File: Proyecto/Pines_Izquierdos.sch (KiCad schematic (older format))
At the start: 7 parts

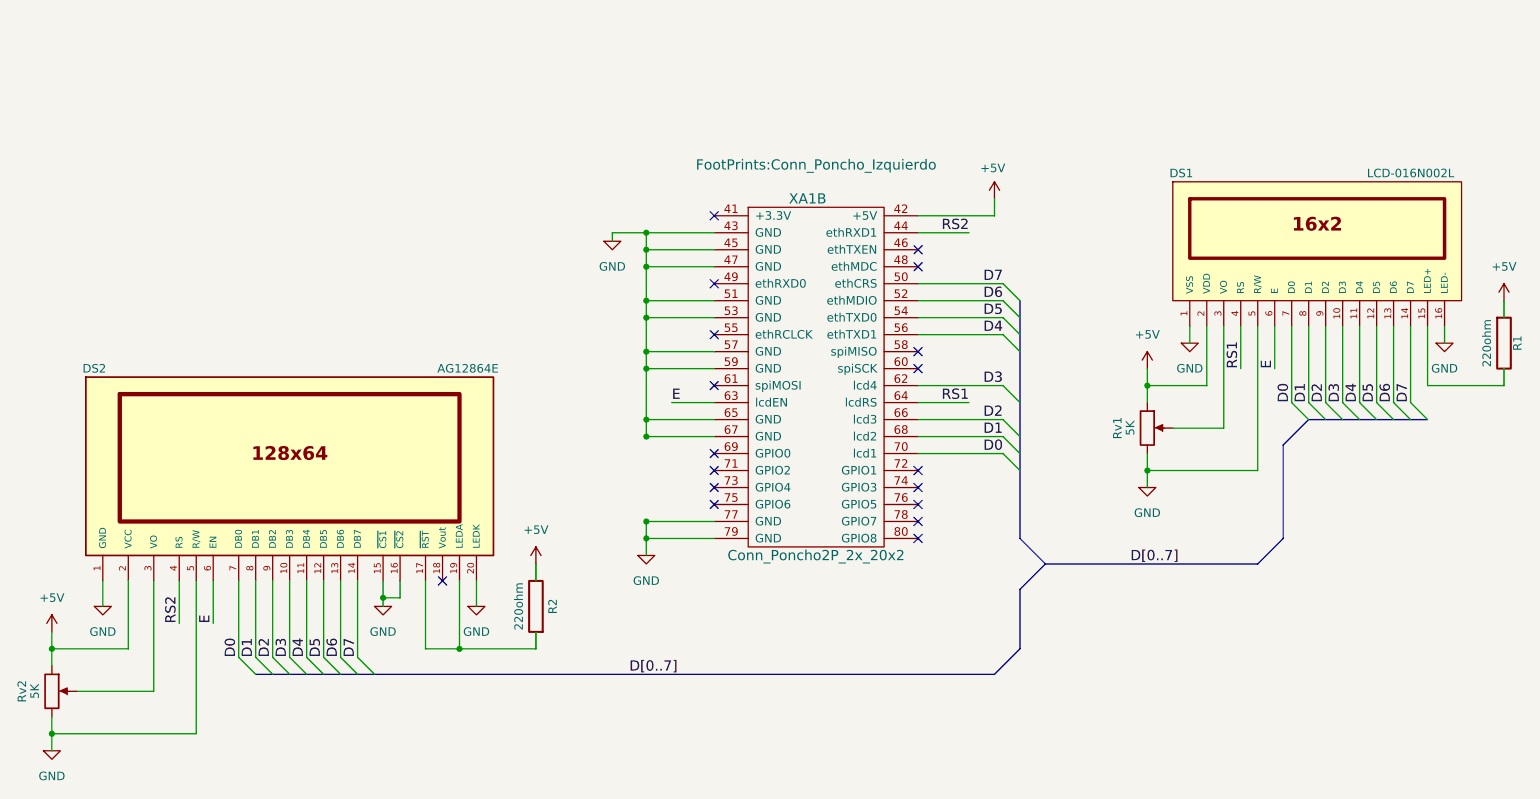
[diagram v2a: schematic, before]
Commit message: Modelos 3D
Se modificaron FootPrints y se agregaron modelos en 3D.
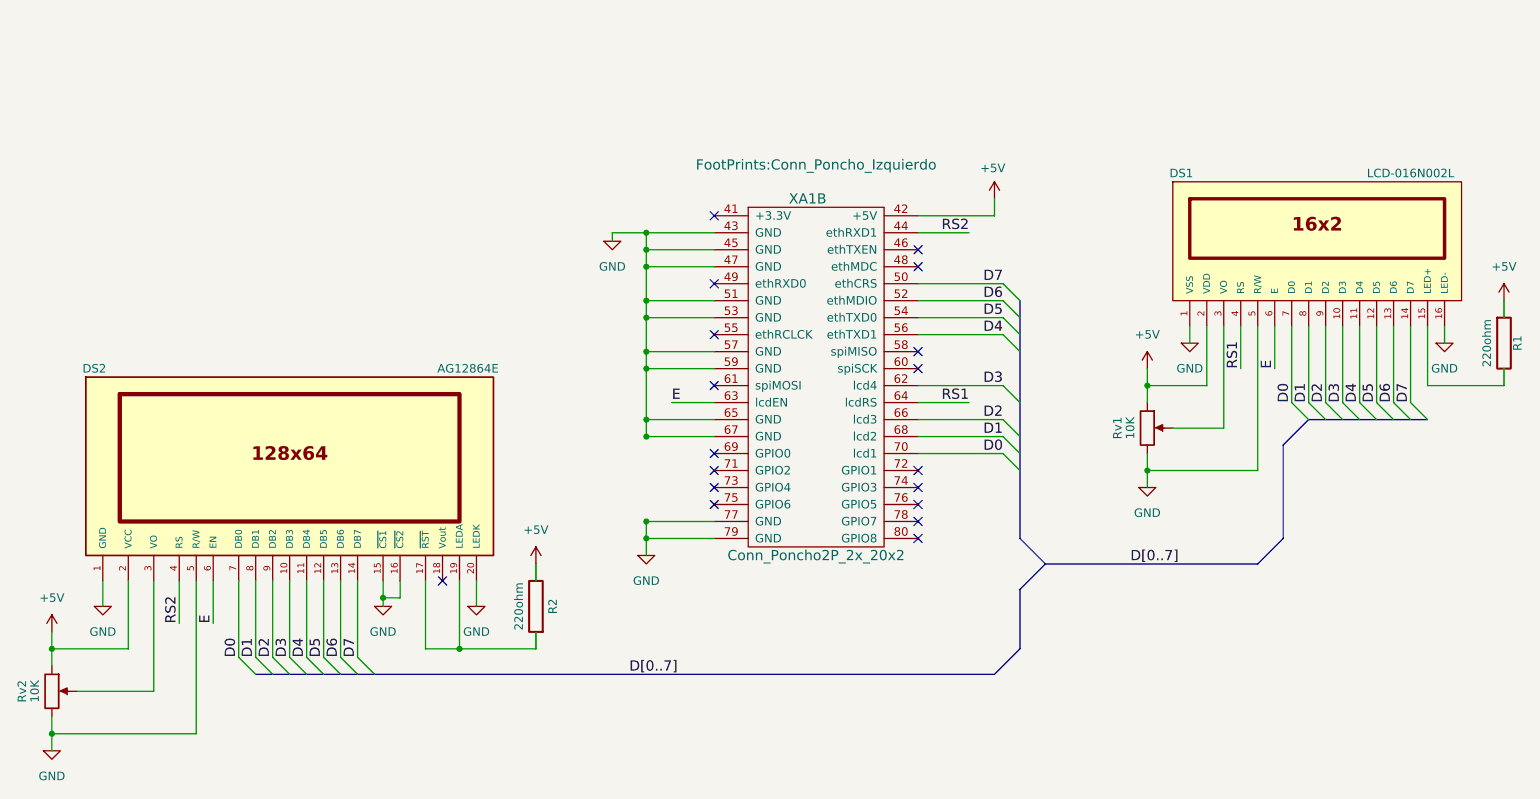
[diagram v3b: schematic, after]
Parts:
- DS1: Desc (none) -> Character LCD Display Module Transmissive 5 x 8 Dots FSTN -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; Digikey# (none) -> NHD-0216K1Z-NS(RGB)-FBW-REV1-ND; Manf (none) -> Newhaven Display Intl; Manf# (none) -> NHD-0216K1Z-NS(RGB)-FBW-REV1
- DS2: Desc (none) -> Graphic LCD Display Module Transmissive STN - Super-Twisted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; Digikey# (none) -> NHD-12864WG-BTMI-V#N-ND; Manf (none) -> Newhaven Display Intl; Manf# (none) -> NHD-12864WG-BTMI-V#N
- R1, R2: Desc (none) -> Resistencia en microprocesador 0.25 W, 1/4 W ±0.5% 220 Ohm 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; Digikey# (none) -> P20941TR-ND; Manf (none) -> Panasonic Electronic Components; Manf# (none) -> ERJ-PB6D2200V
- Rv1, Rv2: value 5K -> 10K; Desc (none) -> 10k Ohm Gang Linear Through Hole Potentiometer None 1 Turn 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; Digikey# (none) -> 3310P-025-103L-ND; Manf (none) -> Bourns Inc.; Manf# (none) -> 3310P-025-103L
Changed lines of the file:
@@
 P 7900 3850
 AR Path="/59239964" Ref="#PWR?"  Part="1"
-AR Path="/591BB8C8/59239964" Ref="#PWR09"  Part="1"
-F 0 "#PWR09" H 7900 3600 50  0001 C CNN
+AR Path="/591BB8C8/59239964" Ref="#PWR08"  Part="1"
+F 0 "#PWR08" H 7900 3600 50  0001 C CNN
 F 1 "GND" H 7900 3700 50  0000 C CNN
 F 2 "" H 7900 3850 50  0001 C CNN
@@
 P 4950 4250
 AR Path="/5923997C" Ref="#PWR?"  Part="1"
-AR Path="/591BB8C8/5923997C" Ref="#PWR010"  Part="1"
-F 0 "#PWR010" H 4950 4000 50  0001 C CNN
+AR Path="/591BB8C8/5923997C" Ref="#PWR09"  Part="1"
+F 0 "#PWR09" H 4950 4000 50  0001 C CNN
 F 1 "GND" H 4950 4100 50  0000 C CNN
 F 2 "" H 4950 4250 50  0001 C CNN
@@
 E
 $Comp
-L +5V #PWR011
+L +5V #PWR010
 U 1 1 59239CAA
 P 7900 3150
-F 0 "#PWR011" H 7900 3000 50  0001 C CNN
+F 0 "#PWR010" H 7900 3000 50  0001 C CNN
 F 1 "+5V" H 7900 3350 50  0000 C CNN
 F 2 "" H 7900 3150 50  0001 C CNN
@@
 P 7900 3500
 F 0 "Rv1" V 7725 3500 50  0000 C CNN
-F 1 "5K" V 7800 3500 50  0000 C CNN
+F 1 "10K" V 7800 3500 50  0000 C CNN
 F 2 "FootPrints:POT_SMD" H 7900 3500 50  0001 C CNN
-F 3 "" H 7900 3500 50  0001 C CNN
+F 3 "3310 Series" H 7900 3500 50  0001 C CNN
+F 4 "Bourns Inc." V 7900 3500 60  0001 C CNN "Manf"
+F 5 "3310P-025-103L" V 7900 3500 60  0001 C CNN "Manf#"
+F 6 "3310P-025-103L-ND" V 7900 3500 60  0001 C CNN "Digikey#"
+F 7 "10k Ohm Gang Linear Through Hole Potentiometer None 1 Turn Conductive Plastic 0.25W, 1/4W PC Pins" V 7900 3500 60  0001 C CNN "Desc"
 	1    7900 3500
 	1    0    0    -1
@@
 F 1 "LCD-016N002L" H 9450 2800 50  0000 C CNN
 F 2 "FootPrints:LCD-016N002L" H 8900 2350 50  0001 C CIN
-F 3 "" H 8900 2400 50  0001 C CNN
+F 3 "NHD-0216K1Z-NS(RGB)-FBW-REV1" H 8900 2400 50  0001 C CNN
+F 4 "Newhaven Display Intl" H 8900 2400 60  0001 C CNN "Manf"
+F 5 "NHD-0216K1Z-NS(RGB)-FBW-REV1" H 8900 2400 60  0001 C CNN "Manf#"
+F 6 "NHD-0216K1Z-NS(RGB)-FBW-REV1-ND" H 8900 2400 60  0001 C CNN "Digikey#"
+F 7 "Character LCD Display Module Transmissive 5 x 8 Dots FSTN - Film Super-Twisted Nematic LED - Red/Green/Blue Parallel 80.00mm x 36.00mm x 13.00mm" H 8900 2400 60  0001 C CNN "Desc"
 	1    8900 2400
 	1    0    0    -1
@@
 P 8150 3000
 AR Path="/5924DD46" Ref="#PWR?"  Part="1"
-AR Path="/591BB8C8/5924DD46" Ref="#PWR012"  Part="1"
-F 0 "#PWR012" H 8150 2750 50  0001 C CNN
+AR Path="/591BB8C8/5924DD46" Ref="#PWR011"  Part="1"
+F 0 "#PWR011" H 8150 2750 50  0001 C CNN
 F 1 "GND" H 8150 2850 50  0000 C CNN
 F 2 "" H 8150 3000 50  0001 C CNN
@@
 D[0..7]
 $Comp
-L +5V #PWR013
+L +5V #PWR012
 U 1 1 5924EC76
 P 10000 2750
-F 0 "#PWR013" H 10000 2600 50  0001 C CNN
+F 0 "#PWR012" H 10000 2600 50  0001 C CNN
 F 1 "+5V" H 10000 2950 50  0000 C CNN
 F 2 "" H 10000 2750 50  0001 C CNN
@@
 P 9650 3000
 AR Path="/5924EC90" Ref="#PWR?"  Part="1"
-AR Path="/591BB8C8/5924EC90" Ref="#PWR014"  Part="1"
-F 0 "#PWR014" H 9650 2750 50  0001 C CNN
+AR Path="/591BB8C8/5924EC90" Ref="#PWR013"  Part="1"
+F 0 "#PWR013" H 9650 2750 50  0001 C CNN
 F 1 "GND" H 9650 2850 50  0000 C CNN
 F 2 "" H 9650 3000 50  0001 C CNN
@@
 P 4750 2400
 AR Path="/5924F240" Ref="#PWR?"  Part="1"
-AR Path="/591BB8C8/5924F240" Ref="#PWR015"  Part="1"
-F 0 "#PWR015" H 4750 2150 50  0001 C CNN
+AR Path="/591BB8C8/5924F240" Ref="#PWR014"  Part="1"
+F 0 "#PWR014" H 4750 2150 50  0001 C CNN
 F 1 "GND" H 4750 2250 50  0000 C CNN
 F 2 "" H 4750 2400 50  0001 C CNN
@@
 F 1 "AG12864E" H 3900 4450 50  0000 C CNN
 F 2 "FootPrints:AG12864E" H 2850 3600 50  0001 C CIN
-F 3 "MGL5128 128x64 Graphic LCD Module - User Manual.pdf" H 2850 3800 50  0001 C CNN
+F 3 "NHD-12864WG-BTMI-V# User Guide" H 2850 3800 50  0001 C CNN
+F 4 "Newhaven Display Intl" H 2850 3800 60  0001 C CNN "Manf"
+F 5 "NHD-12864WG-BTMI-V#N" H 2850 3800 60  0001 C CNN "Manf#"
+F 6 "NHD-12864WG-BTMI-V#N-ND" H 2850 3800 60  0001 C CNN "Digikey#"
+F 7 "Graphic LCD Display Module Transmissive STN - Super-Twisted Nematic Parallel, 8-Bit 128 x 64" H 2850 3800 60  0001 C CNN "Desc"
 	1    2850 3800
 	1    0    0    -1
@@
 P 1750 4550
 AR Path="/59262698" Ref="#PWR?"  Part="1"
-AR Path="/591BB8C8/59262698" Ref="#PWR016"  Part="1"
-F 0 "#PWR016" H 1750 4300 50  0001 C CNN
+AR Path="/591BB8C8/59262698" Ref="#PWR015"  Part="1"
+F 0 "#PWR015" H 1750 4300 50  0001 C CNN
 F 1 "GND" H 1750 4400 50  0000 C CNN
 F 2 "" H 1750 4550 50  0001 C CNN
@@
 P 1450 5050
 F 0 "Rv2" V 1275 5050 50  0000 C CNN
-F 1 "5K" V 1350 5050 50  0000 C CNN
+F 1 "10K" V 1350 5050 50  0000 C CNN
 F 2 "FootPrints:POT_SMD" H 1450 5050 50  0001 C CNN
-F 3 "" H 1450 5050 50  0001 C CNN
+F 3 "3310 Series" H 1450 5050 50  0001 C CNN
+F 4 "Bourns Inc." V 1450 5050 60  0001 C CNN "Manf"
+F 5 "3310P-025-103L" V 1450 5050 60  0001 C CNN "Manf#"
+F 6 "3310P-025-103L-ND" V 1450 5050 60  0001 C CNN "Digikey#"
+F 7 "10k Ohm Gang Linear Through Hole Potentiometer None 1 Turn Conductive Plastic 0.25W, 1/4W PC Pins" V 1450 5050 60  0001 C CNN "Desc"
 	1    1450 5050
 	1    0    0    -1
 $EndComp
 $Comp
-L +5V #PWR017
+L +5V #PWR016
 U 1 1 5926296A
 P 1450 4700
-F 0 "#PWR017" H 1450 4550 50  0001 C CNN
+F 0 "#PWR016" H 1450 4550 50  0001 C CNN
 F 1 "+5V" H 1450 4900 50  0000 C CNN
 F 2 "" H 1450 4700 50  0001 C CNN
@@
 P 1450 5400
 AR Path="/59262A0A" Ref="#PWR?"  Part="1"
-AR Path="/591BB8C8/59262A0A" Ref="#PWR018"  Part="1"
-F 0 "#PWR018" H 1450 5150 50  0001 C CNN
+AR Path="/591BB8C8/59262A0A" Ref="#PWR017"  Part="1"
+F 0 "#PWR017" H 1450 5150 50  0001 C CNN
 F 1 "GND" H 1450 5250 50  0000 C CNN
 F 2 "" H 1450 5400 50  0001 C CNN
@@
 P 3950 4550
 AR Path="/592653AA" Ref="#PWR?"  Part="1"
-AR Path="/591BB8C8/592653AA" Ref="#PWR019"  Part="1"
-F 0 "#PWR019" H 3950 4300 50  0001 C CNN
+AR Path="/591BB8C8/592653AA" Ref="#PWR018"  Part="1"
+F 0 "#PWR018" H 3950 4300 50  0001 C CNN
 F 1 "GND" H 3950 4400 50  0000 C CNN
 F 2 "" H 3950 4550 50  0001 C CNN
@@
 $EndComp
 $Comp
-L +5V #PWR020
+L +5V #PWR019
 U 1 1 592653C8
 P 4300 4300
-F 0 "#PWR020" H 4300 4150 50  0001 C CNN
+F 0 "#PWR019" H 4300 4150 50  0001 C CNN
 F 1 "+5V" H 4300 4500 50  0000 C CNN
 F 2 "" H 4300 4300 50  0001 C CNN
@@
 F 1 "220ohm" V 4400 4550 50  0000 C CNN
 F 2 "FootPrints:R_0805_HandSoldering" V 4230 4550 50  0001 C CNN
-F 3 "" H 4300 4550 50  0001 C CNN
+F 3 "Fixed Resistors Prod Catalog" H 4300 4550 50  0001 C CNN
+F 4 "Panasonic Electronic Components" V 4300 4550 60  0001 C CNN "Manf"
+F 5 "ERJ-PB6D2200V" V 4300 4550 60  0001 C CNN "Manf#"
+F 6 "P20941TR-ND" V 4300 4550 60  0001 C CNN "Digikey#"
+F 7 "Resistencia en microprocesador 0.25 W, 1/4 W ±0.5% 220 Ohm AEC-Q200 automotriz, protección contra impulsos Película gruesa 0805 (2012 métrico)" V 4300 4550 60  0001 C CNN "Desc"
 	1    4300 4550
 	-1   0    0    1
@@
 F 1 "220ohm" V 9900 3000 50  0000 C CNN
 F 2 "FootPrints:R_0805_HandSoldering" V 9930 3000 50  0001 C CNN
-F 3 "" H 10000 3000 50  0001 C CNN
+F 3 "Fixed Resistors Prod Catalog" H 10000 3000 50  0001 C CNN
+F 4 "Panasonic Electronic Components" V 10000 3000 60  0001 C CNN "Manf"
+F 5 "ERJ-PB6D2200V" V 10000 3000 60  0001 C CNN "Manf#"
+F 6 "P20941TR-ND" V 10000 3000 60  0001 C CNN "Digikey#"
+F 7 "Resistencia en microprocesador 0.25 W, 1/4 W ±0.5% 220 Ohm AEC-Q200 automotriz, protección contra impulsos Película gruesa 0805 (2012 métrico)" V 10000 3000 60  0001 C CNN "Desc"
 	1    10000 3000
 	1    0    0    -1
@@
 P 3400 4550
 AR Path="/5926E76E" Ref="#PWR?"  Part="1"
-AR Path="/591BB8C8/5926E76E" Ref="#PWR021"  Part="1"
-F 0 "#PWR021" H 3400 4300 50  0001 C CNN
+AR Path="/591BB8C8/5926E76E" Ref="#PWR020"  Part="1"
+F 0 "#PWR020" H 3400 4300 50  0001 C CNN
 F 1 "GND" H 3400 4400 50  0000 C CNN
 F 2 "" H 3400 4550 50  0001 C CNN
@@
 	7000 2250 6550 2250
 $Comp
-L +5V #PWR022
+L +5V #PWR021
 U 1 1 592A62F7
 P 7000 2150
-F 0 "#PWR022" H 7000 2000 50  0001 C CNN
+F 0 "#PWR021" H 7000 2000 50  0001 C CNN
 F 1 "+5V" H 6990 2330 50  0000 C CNN
 F 2 "" H 7000 2150 50  0001 C CNN

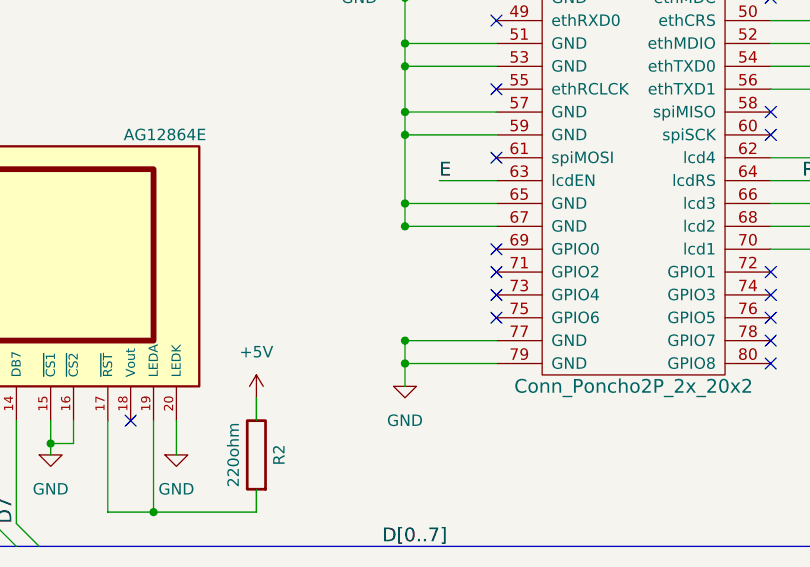
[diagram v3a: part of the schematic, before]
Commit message: Ruteo y 3D
Se realizó el ruteo completo y se agregaron modelos 3D
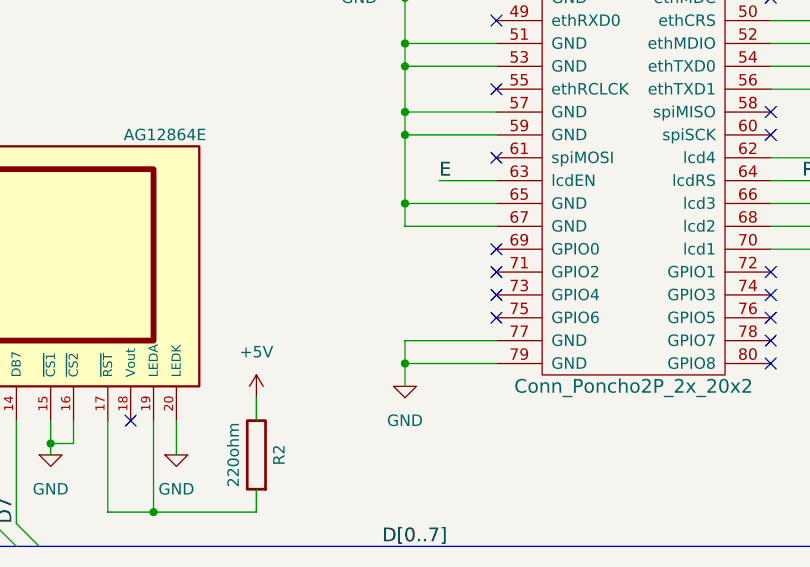
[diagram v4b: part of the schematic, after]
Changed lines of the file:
@@
 LIBS:display
 LIBS:Poncho_Esqueleto
+LIBS:conn
 LIBS:Poncho_Educativo_v2.0-cache
 EELAYER 25 0
@@
 Date "2017-05-22"
 Rev ""
-Comp "Curso - Diseño de PCB"
-Comment1 "Autor Esquemático: Ing. Jhon Jairo Vargas Yaya"
-Comment2 ""
-Comment3 ""
-Comment4 ""
+Comp "CESE - Diseño de PCB"
+Comment1 "Licencia del proyecto: BSD 2 - Archivo: LICENSE"
+Comment2 "Autor del Poncho: Ing. Jhon Jairo Vargas Yaya"
+Comment3 "Autores y Licencia del template (Diego Brengi - UNLaM)"
+Comment4 "Revisor: Juan Carlos Suarez"
 $EndDescr
 $Comp
@@
 P 7900 3850
 AR Path="/59239964" Ref="#PWR?"  Part="1"
-AR Path="/591BB8C8/59239964" Ref="#PWR08"  Part="1"
-F 0 "#PWR08" H 7900 3600 50  0001 C CNN
+AR Path="/591BB8C8/59239964" Ref="#PWR09"  Part="1"
+F 0 "#PWR09" H 7900 3600 50  0001 C CNN
 F 1 "GND" H 7900 3700 50  0000 C CNN
 F 2 "" H 7900 3850 50  0001 C CNN
@@
 P 4950 4250
 AR Path="/5923997C" Ref="#PWR?"  Part="1"
-AR Path="/591BB8C8/5923997C" Ref="#PWR09"  Part="1"
-F 0 "#PWR09" H 4950 4000 50  0001 C CNN
+AR Path="/591BB8C8/5923997C" Ref="#PWR010"  Part="1"
+F 0 "#PWR010" H 4950 4000 50  0001 C CNN
 F 1 "GND" H 4950 4100 50  0000 C CNN
 F 2 "" H 4950 4250 50  0001 C CNN
@@
 E
 $Comp
-L +5V #PWR010
+L +5V #PWR011
 U 1 1 59239CAA
 P 7900 3150
-F 0 "#PWR010" H 7900 3000 50  0001 C CNN
+F 0 "#PWR011" H 7900 3000 50  0001 C CNN
 F 1 "+5V" H 7900 3350 50  0000 C CNN
 F 2 "" H 7900 3150 50  0001 C CNN
@@
 P 8150 3000
 AR Path="/5924DD46" Ref="#PWR?"  Part="1"
-AR Path="/591BB8C8/5924DD46" Ref="#PWR011"  Part="1"
-F 0 "#PWR011" H 8150 2750 50  0001 C CNN
+AR Path="/591BB8C8/5924DD46" Ref="#PWR012"  Part="1"
+F 0 "#PWR012" H 8150 2750 50  0001 C CNN
 F 1 "GND" H 8150 2850 50  0000 C CNN
 F 2 "" H 8150 3000 50  0001 C CNN
@@
 D[0..7]
 $Comp
-L +5V #PWR012
+L +5V #PWR013
 U 1 1 5924EC76
 P 10000 2750
-F 0 "#PWR012" H 10000 2600 50  0001 C CNN
+F 0 "#PWR013" H 10000 2600 50  0001 C CNN
 F 1 "+5V" H 10000 2950 50  0000 C CNN
 F 2 "" H 10000 2750 50  0001 C CNN
@@
 P 9650 3000
 AR Path="/5924EC90" Ref="#PWR?"  Part="1"
-AR Path="/591BB8C8/5924EC90" Ref="#PWR013"  Part="1"
-F 0 "#PWR013" H 9650 2750 50  0001 C CNN
+AR Path="/591BB8C8/5924EC90" Ref="#PWR014"  Part="1"
+F 0 "#PWR014" H 9650 2750 50  0001 C CNN
 F 1 "GND" H 9650 2850 50  0000 C CNN
 F 2 "" H 9650 3000 50  0001 C CNN
@@
 P 4750 2400
 AR Path="/5924F240" Ref="#PWR?"  Part="1"
-AR Path="/591BB8C8/5924F240" Ref="#PWR014"  Part="1"
-F 0 "#PWR014" H 4750 2150 50  0001 C CNN
+AR Path="/591BB8C8/5924F240" Ref="#PWR015"  Part="1"
+F 0 "#PWR015" H 4750 2150 50  0001 C CNN
 F 1 "GND" H 4750 2250 50  0000 C CNN
 F 2 "" H 4750 2400 50  0001 C CNN
@@
 P 1750 4550
 AR Path="/59262698" Ref="#PWR?"  Part="1"
-AR Path="/591BB8C8/59262698" Ref="#PWR015"  Part="1"
-F 0 "#PWR015" H 1750 4300 50  0001 C CNN
+AR Path="/591BB8C8/59262698" Ref="#PWR016"  Part="1"
+F 0 "#PWR016" H 1750 4300 50  0001 C CNN
 F 1 "GND" H 1750 4400 50  0000 C CNN
 F 2 "" H 1750 4550 50  0001 C CNN
@@
 $EndComp
 $Comp
-L +5V #PWR016
+L +5V #PWR017
 U 1 1 5926296A
 P 1450 4700
-F 0 "#PWR016" H 1450 4550 50  0001 C CNN
+F 0 "#PWR017" H 1450 4550 50  0001 C CNN
 F 1 "+5V" H 1450 4900 50  0000 C CNN
 F 2 "" H 1450 4700 50  0001 C CNN
@@
 P 1450 5400
 AR Path="/59262A0A" Ref="#PWR?"  Part="1"
-AR Path="/591BB8C8/59262A0A" Ref="#PWR017"  Part="1"
-F 0 "#PWR017" H 1450 5150 50  0001 C CNN
+AR Path="/591BB8C8/59262A0A" Ref="#PWR018"  Part="1"
+F 0 "#PWR018" H 1450 5150 50  0001 C CNN
 F 1 "GND" H 1450 5250 50  0000 C CNN
 F 2 "" H 1450 5400 50  0001 C CNN
@@
 D7
 Connection ~ 4950 4150
-Connection ~ 4950 4050
-Connection ~ 4950 3550
 Connection ~ 4950 3450
 Connection ~ 4950 3150
@@
 P 3950 4550
 AR Path="/592653AA" Ref="#PWR?"  Part="1"
-AR Path="/591BB8C8/592653AA" Ref="#PWR018"  Part="1"
-F 0 "#PWR018" H 3950 4300 50  0001 C CNN
+AR Path="/591BB8C8/592653AA" Ref="#PWR019"  Part="1"
+F 0 "#PWR019" H 3950 4300 50  0001 C CNN
 F 1 "GND" H 3950 4400 50  0000 C CNN
 F 2 "" H 3950 4550 50  0001 C CNN
@@
 $EndComp
 $Comp
-L +5V #PWR019
+L +5V #PWR020
 U 1 1 592653C8
 P 4300 4300
-F 0 "#PWR019" H 4300 4150 50  0001 C CNN
+F 0 "#PWR020" H 4300 4150 50  0001 C CNN
 F 1 "+5V" H 4300 4500 50  0000 C CNN
 F 2 "" H 4300 4300 50  0001 C CNN
@@
 P 3400 4550
 AR Path="/5926E76E" Ref="#PWR?"  Part="1"
-AR Path="/591BB8C8/5926E76E" Ref="#PWR020"  Part="1"
-F 0 "#PWR020" H 3400 4300 50  0001 C CNN
+AR Path="/591BB8C8/5926E76E" Ref="#PWR021"  Part="1"
+F 0 "#PWR021" H 3400 4300 50  0001 C CNN
 F 1 "GND" H 3400 4400 50  0000 C CNN
 F 2 "" H 3400 4550 50  0001 C CNN
@@
 	7000 2250 6550 2250
 $Comp
-L +5V #PWR021
+L +5V #PWR022
 U 1 1 592A62F7
 P 7000 2150
-F 0 "#PWR021" H 7000 2000 50  0001 C CNN
+F 0 "#PWR022" H 7000 2000 50  0001 C CNN
 F 1 "+5V" H 6990 2330 50  0000 C CNN
 F 2 "" H 7000 2150 50  0001 C CNN
